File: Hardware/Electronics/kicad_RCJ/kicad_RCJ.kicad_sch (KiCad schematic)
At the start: 30 parts, among them J1 Raspberry_Pi_2_3, U23 TCS34725, U24 APDS9960

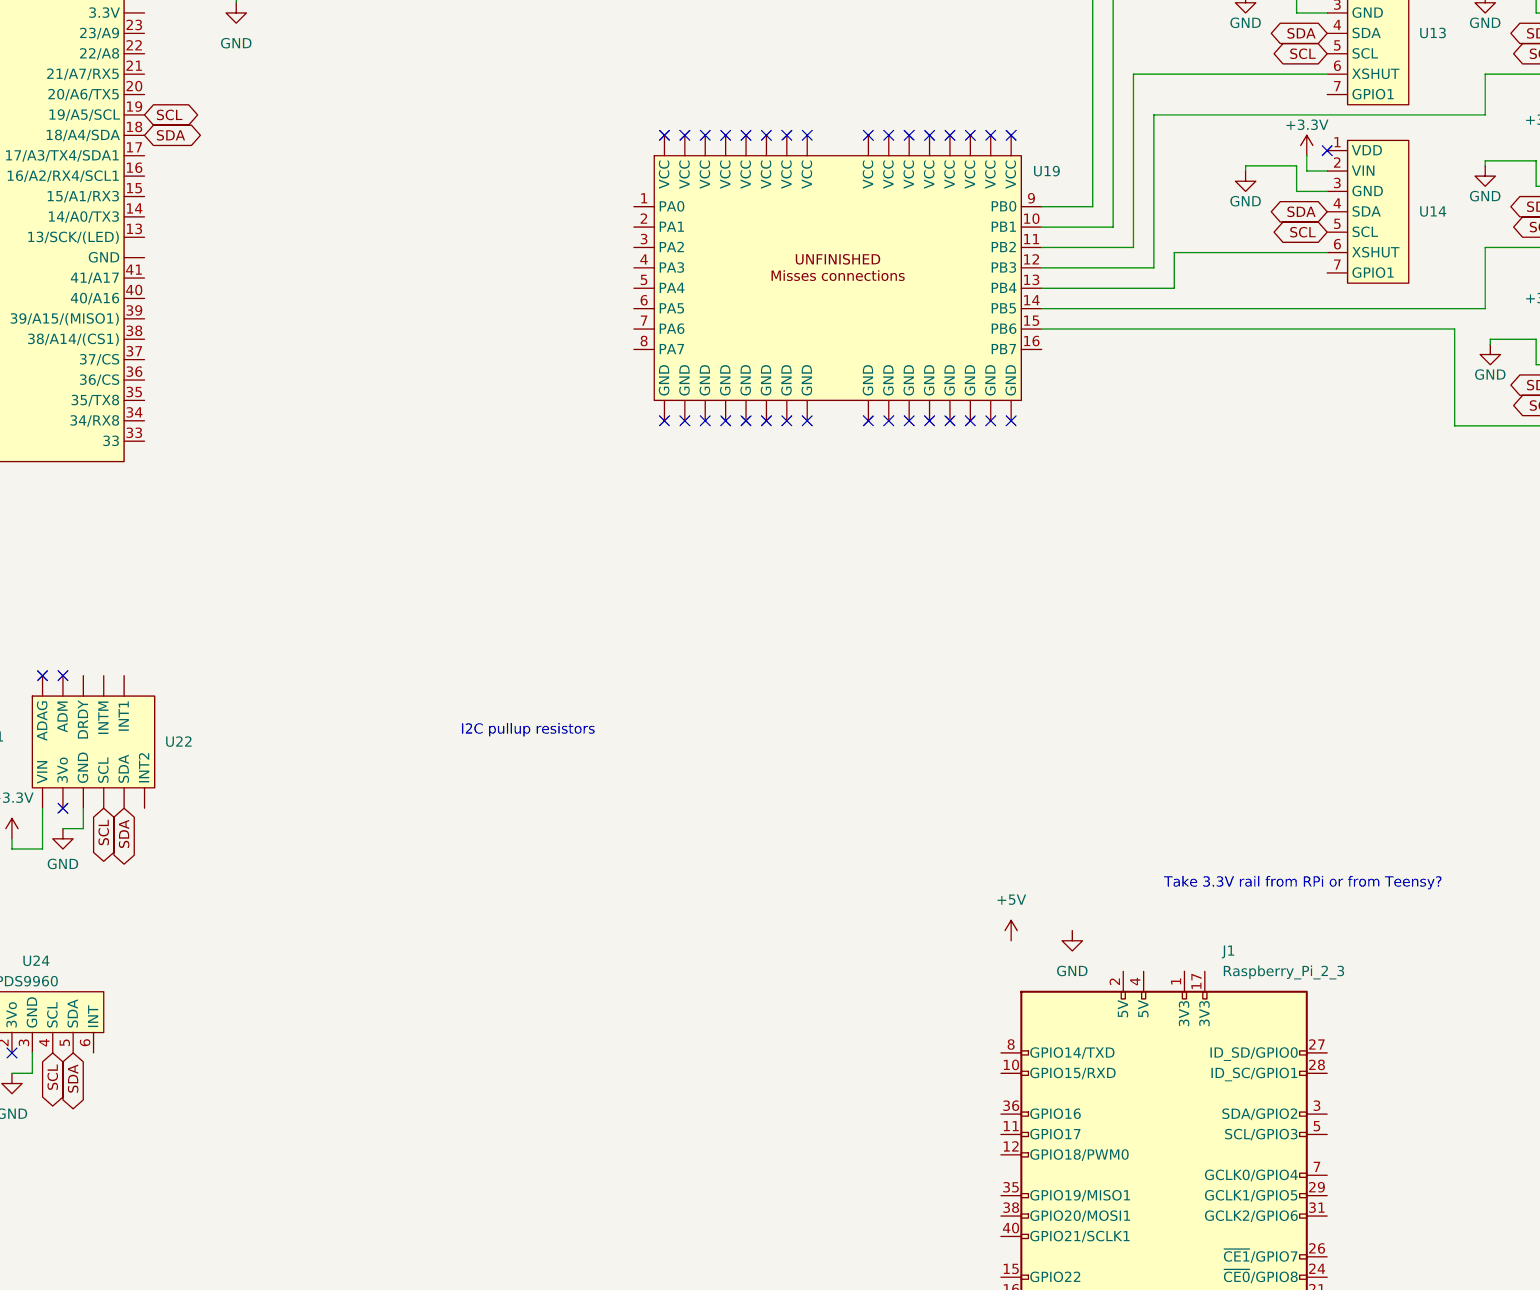
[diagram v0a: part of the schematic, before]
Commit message: added I2C pullup resistors and I2C between teensy and pi
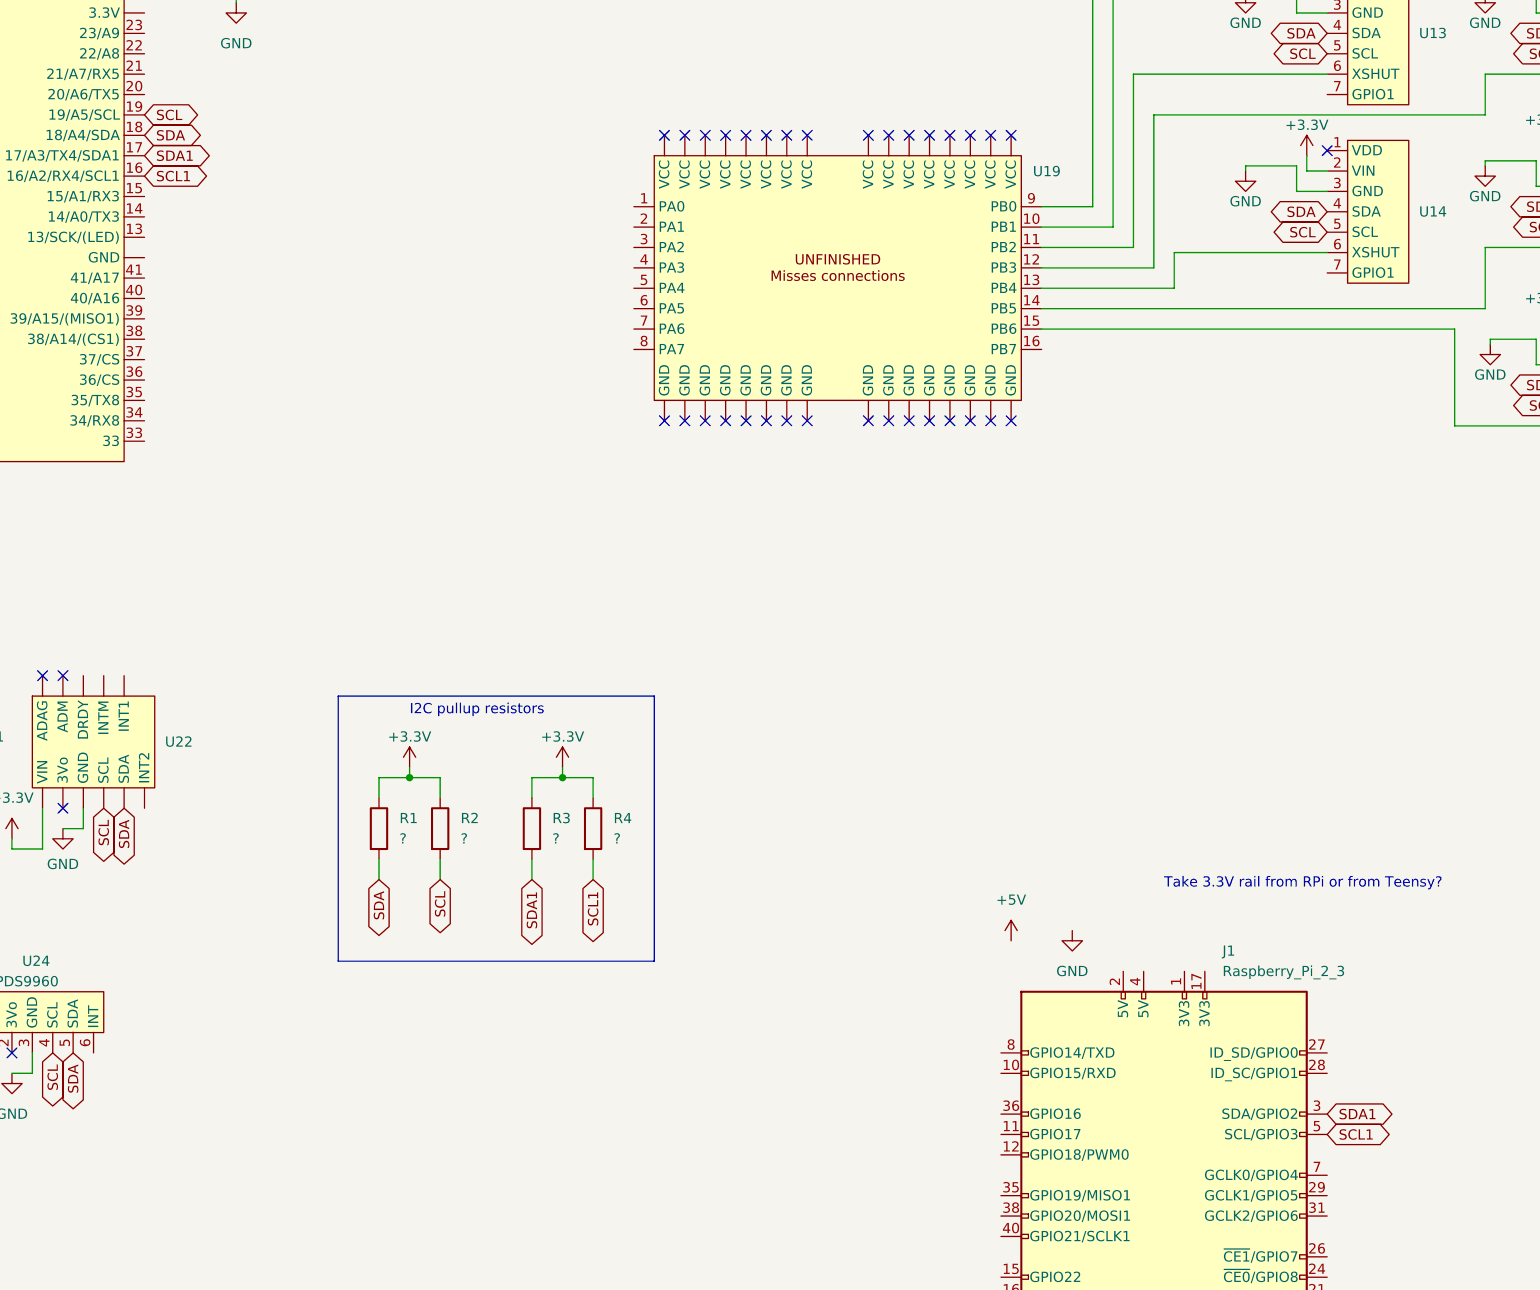
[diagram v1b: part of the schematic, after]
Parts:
- added R1, R2, R3, R4: ?, symbol Device:R
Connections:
- net +3.3V: now also R1.1, R2.1, R3.1, R4.1
- net SCL: now also R2.2
- net SDA: now also R1.2
- net SDA1: now reaches J1.3 (SDA/GPIO2)
- net SDA1: now also U6.17 (17/A3/TX4/SDA1), R3.2
- net SCL1: now reaches J1.5 (SCL/GPIO3)
- net SCL1: now also U6.16 (16/A2/RX4/SCL1), R4.2

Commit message: added bump switches and colour sensing and did general cleanup and organization
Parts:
- added R10, R12, R6, R8: R?, symbol Device:R
- added R11, R5, R7, R9: R_Photo, symbol Device:R_Photo
- added S1, S2, S3, S4: ~, symbol RCJ_parts:SW_limit
- R1, R2, R3, R4: value ? -> R?
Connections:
- net +3.3V: now also R11.1, R5.1, R7.1, R9.1
- net GND: now also R10.2, R12.2, R6.2, R8.2, S1.1 (C), S2.1 (C), S3.1 (C), S4.1 (C)
- net at U6.14 (14/A0/TX3): now also R10.1, R9.2
- net at U6.15 (15/A1/RX3): now also R11.2, R12.1
- net at U6.33: now also S4.3 (NO)
- net at U6.34 (34/RX8): now also S3.3 (NO)
- net at U6.35 (35/TX8): now also S2.3 (NO)
- net at U6.36 (36/CS): now also S1.3 (NO)
- net at U6.40 (40/A16): now also R5.2, R6.1
- net at U6.41 (41/A17): now also R7.2, R8.1
- no-connect marks 74 -> 78
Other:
- note added: "Bump switches"
- note added: "Colour sensing"
- note added: "Extras"
- note added: "Fuses, switches and voltage measurement?"
- note added: "IMU"
- note added: "Motors"
- note added: "Power"
- note added: "Should they be connected to the IO expander or directly to the teensy?"
- note added: "Superteams modules"
- note added: "Take 3.3V rail from RPi, from Teensy or from separate converter?"
- note added: "ToF"
- note removed: "Take 3.3V rail from RPi or from Teensy?"
- moved on the sheet: M1, M2, M3, M4, R1, R2, R3, R4, U1, U10, U11, U2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
